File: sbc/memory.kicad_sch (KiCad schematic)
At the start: 6 parts, among them U10 AT27C256R, U11 IS61C5128AS-25QLI, U8 ATF22V10C, U9 ATF22V10C

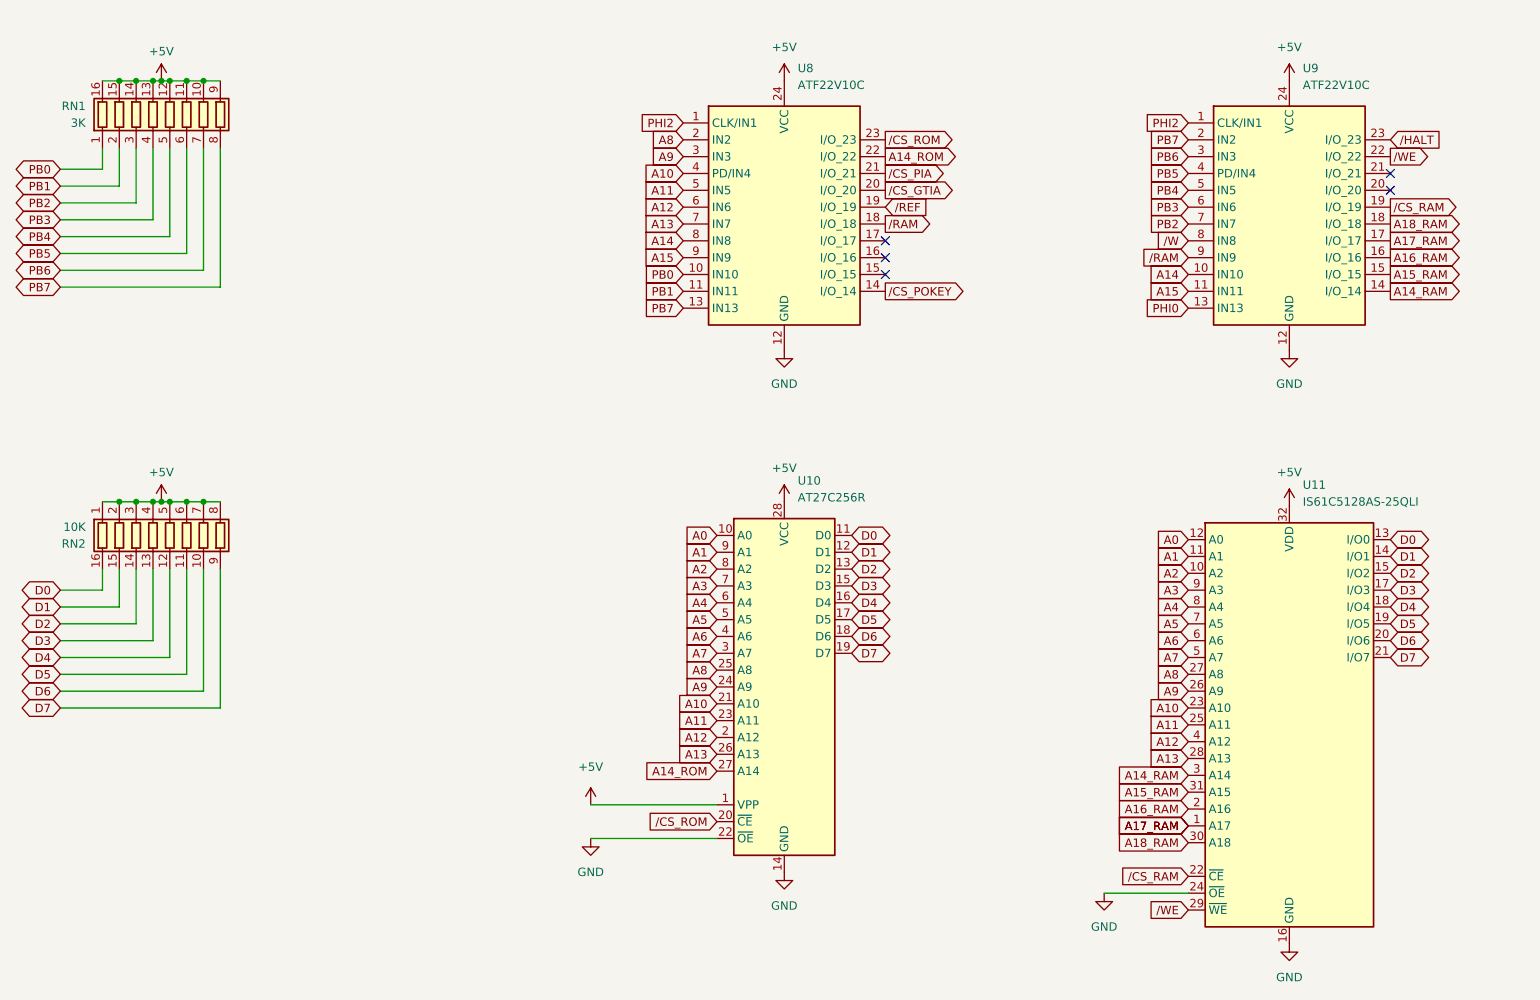
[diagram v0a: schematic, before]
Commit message: SBC v1.1
PCB fixes/changes:

  - Permanently power voltage translators
  - Conservatively specified a slower SRAM (the previous/faster SRAM does actually work fine)
  - RMU: Speculatively provided unbuffered PHI0 input and OE output (not actually needed)
  - Add pullups to open drain GTIA outputs
  - Plot selected values on silk screen
  - Accommodate KiCad 7 upgrade

- PLD changes:
  - Fix AMU logic
  - Fix RMU (unbuffered PHI0 and OE output not needed)

- QTPY firmware:
  - add soft power on/off support (Ctrl-F12)
  - reflects switched power and usb state in the neopixel
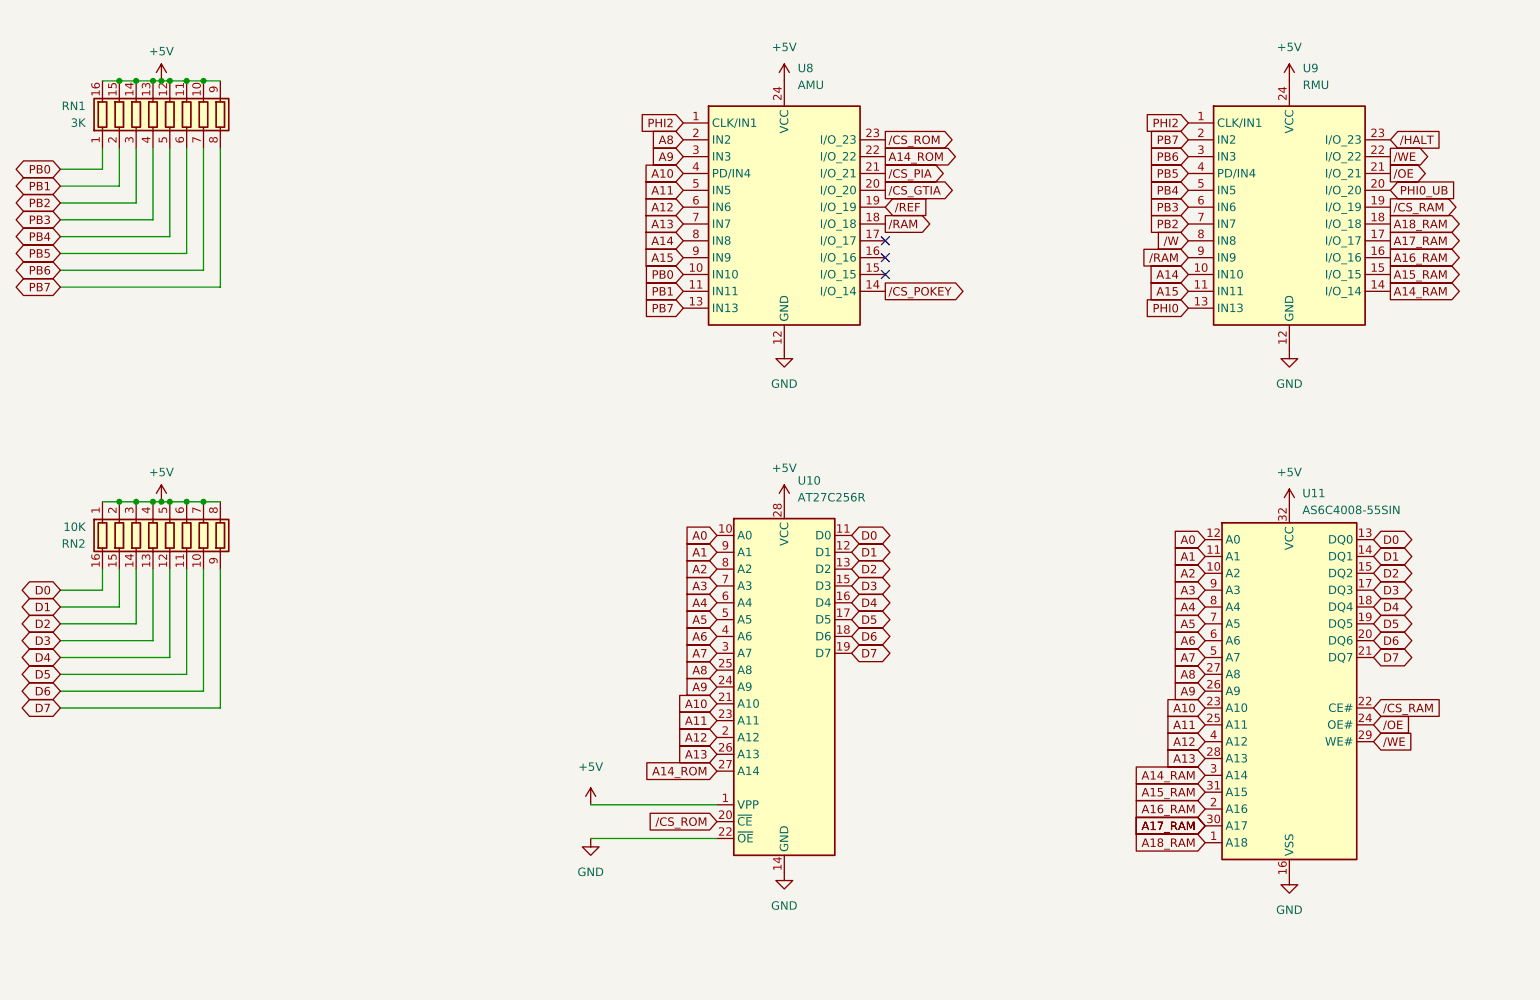
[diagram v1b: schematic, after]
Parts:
- removed U11: IS61C5128AS-25QLI, Package_SO:SSOP-32_11.305x20.495mm_P1.27mm, symbol Memory_RAM:IS61C5128AS-25QLI
- added U11: AS6C4008-55SIN, Package_SO:SSOP-32_11.305x20.495mm_P1.27mm, symbol Memory_RAM:AS6C4008-55PCN
- U8: value ATF22V10C -> AMU
- U9: value ATF22V10C -> RMU
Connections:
- net +5V: now also U11.32 (VCC)
- net A0: now also U11.12 (A0)
- net A1: now also U11.11 (A1)
- net A10: now also U11.23 (A10)
- net A11: now also U11.25 (A11)
- net A12: now also U11.4 (A12)
- net A13: now also U11.28 (A13)
- net A14_RAM: now also U11.3 (A14)
- net A15_RAM: now also U11.31 (A15)
- net A16_RAM: now also U11.2 (A16)
- net A17_RAM: now also U11.30 (A17)
- net A18_RAM: now also U11.1 (A18)
- net A2: now also U11.10 (A2)
- net A3: now also U11.9 (A3)
- net A4: now also U11.8 (A4)
- net A5: now also U11.7 (A5)
- net A6: now also U11.6 (A6)
- net A7: now also U11.5 (A7)
- net A8: now also U11.27 (A8)
- net A9: now also U11.26 (A9)
- net D0: now also U11.13 (DQ0)
- net D1: now also U11.14 (DQ1)
- net D2: now also U11.15 (DQ2)
- net D3: now also U11.17 (DQ3)
- net D4: now also U11.18 (DQ4)
- net D5: now also U11.19 (DQ5)
- net D6: now also U11.20 (DQ6)
- net D7: now also U11.21 (DQ7)
- net GND: now also U11.16 (VSS)
- net /CS_RAM: now also U11.22 (CE#)
- net /WE: now also U11.29 (WE#)
- net PHI0_UB: now reaches U9.20 (I/O_20)
- net /OE: now reaches U9.21 (I/O_21)
- net /OE: now also U11.24 (OE#)
- no-connect marks 5 -> 3

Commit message: SBC v1.2
SBC fixes/changes:

  - S-Video:
    - Fix S-Video footprint (Y and C swapped, and GNDs swapped) and adapt schematic to match
    - Wire S-Video grounds to AVA header instead of directly to (digital) GND
  - Audio:
    - Wire Audio-Out ground to AVA header
    - Drop SIO audio
    - Pullup open drain pokey audio
  - AMU/RMU:
    - Connect ROM and RAM OE to GND
    - Reserve AMU pin for "IO"
    - Reserve RMU pin for "antic" (registered halt)
    - Support for separate Antic banking (clock RMU with /phi2)
    - Supoprt 130XE and 320XE (compy)
  - Add the option for a resistor between OSC, PHI0 buffer and PHI2 buffer (to reduce over/under-shoot)
  - Invert CA2 (a PNP transistor on the Atari 800 XL inverts this signal)

Additions:

  - SBC Audio/Video board
  - SBC Case
  - SBC SD board

Stylize the complete system as "SFF 320XE".
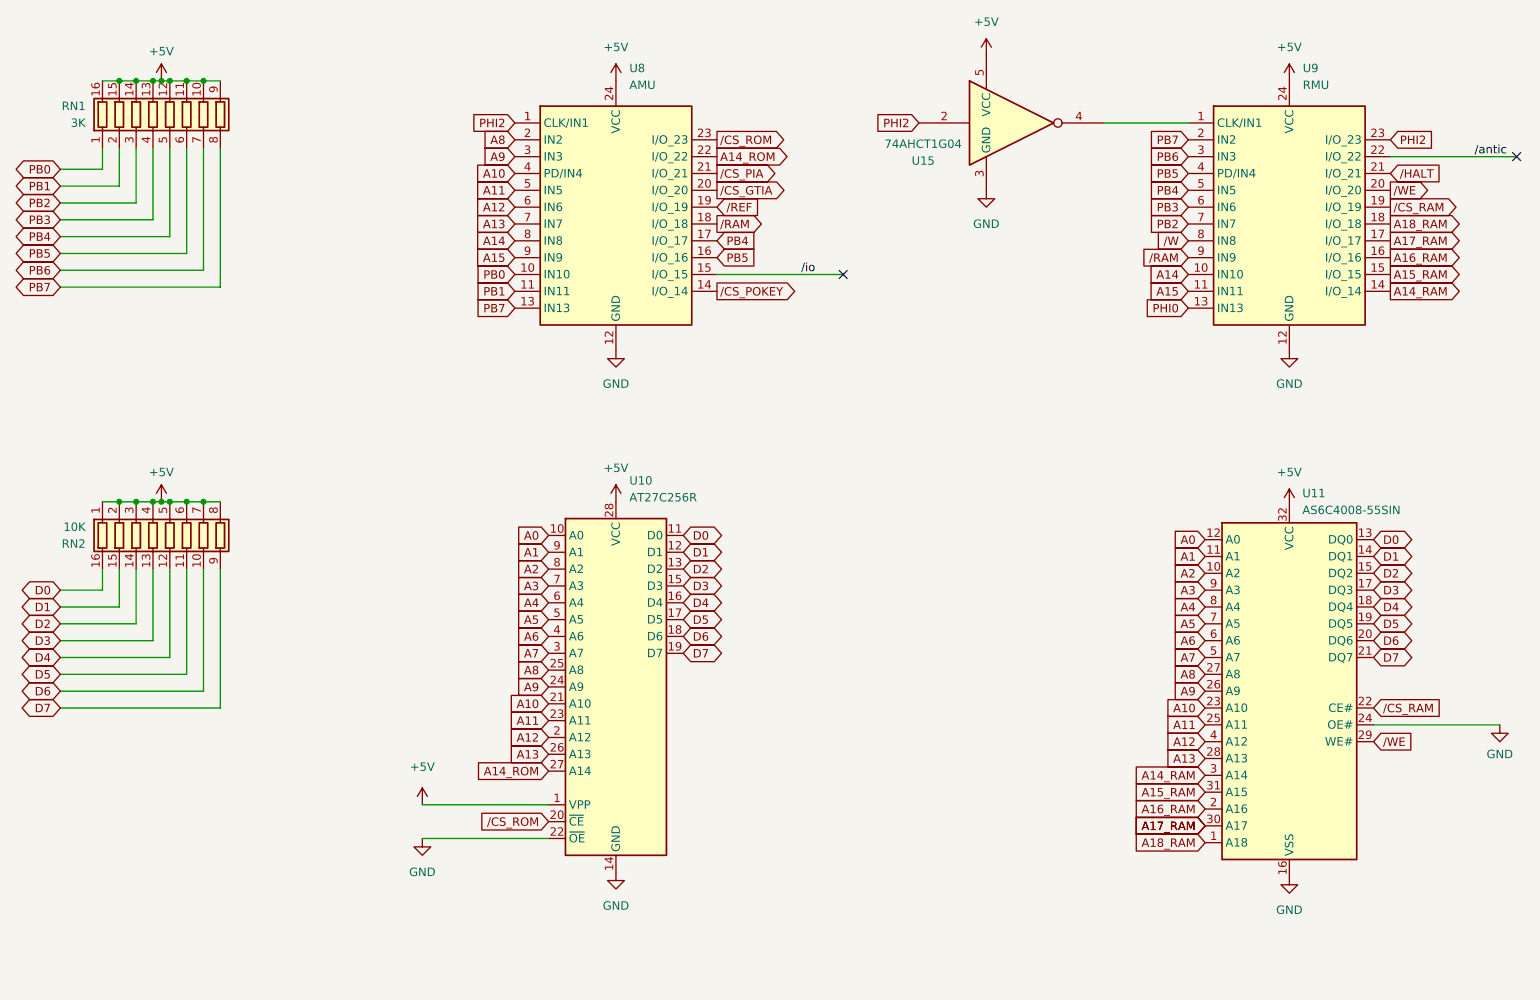
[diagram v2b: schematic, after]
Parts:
- added U15: 74AHCT1G04, Package_TO_SOT_SMD:SOT-23-5_HandSoldering, symbol 74xGxx:74AHCT1G04
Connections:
- net PHI0_UB is gone; now on net /WE: U9.20 (I/O_20)
- net +5V: now also U15.5 (VCC)
- net GND: now also U11.24 (OE#), U15.3 (GND)
- net PB4: now also U8.17 (I/O_17)
- net PB5: now also U8.16 (I/O_16)
- net PHI2: now also U9.23 (I/O_23), U15.2; no longer U9.1 (CLK/IN1)
- net /HALT: now also U9.21 (I/O_21); no longer U9.23 (I/O_23)
- net /WE: no longer U9.22 (I/O_22)
- net /io: now reaches U8.15 (I/O_15)
- removed net /OE: U11.24 (OE#), U9.21 (I/O_21)
- new net: U15.4, U9.1 (CLK/IN1)
- new net /antic: U9.22 (I/O_22)
- no-connect marks 3 -> 2
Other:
- moved on the sheet: U10, U8

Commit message: SBC v1.3
Motherboard updates:

  - KiCad 9 upgrade
  - USB-C power connector
  - Replace EOL resistor packs with discrete SMD resistors
  - Power/enable voltage translators from switched 5V
  - Fix motor signal pullup
  - Eliminate loop in phi2 traces
  - Thicker clock signal traces

SD card adapter updates:

  - KiCad 9 upgrade
  - Power/enable voltage translator from switched 5V and the eliminate unnecessary SIO pullups

Audio/Video adapter updates:

  - KiCad 9 upgrade
  - No functional changes, gerbers not regenerated, cleaned up bom
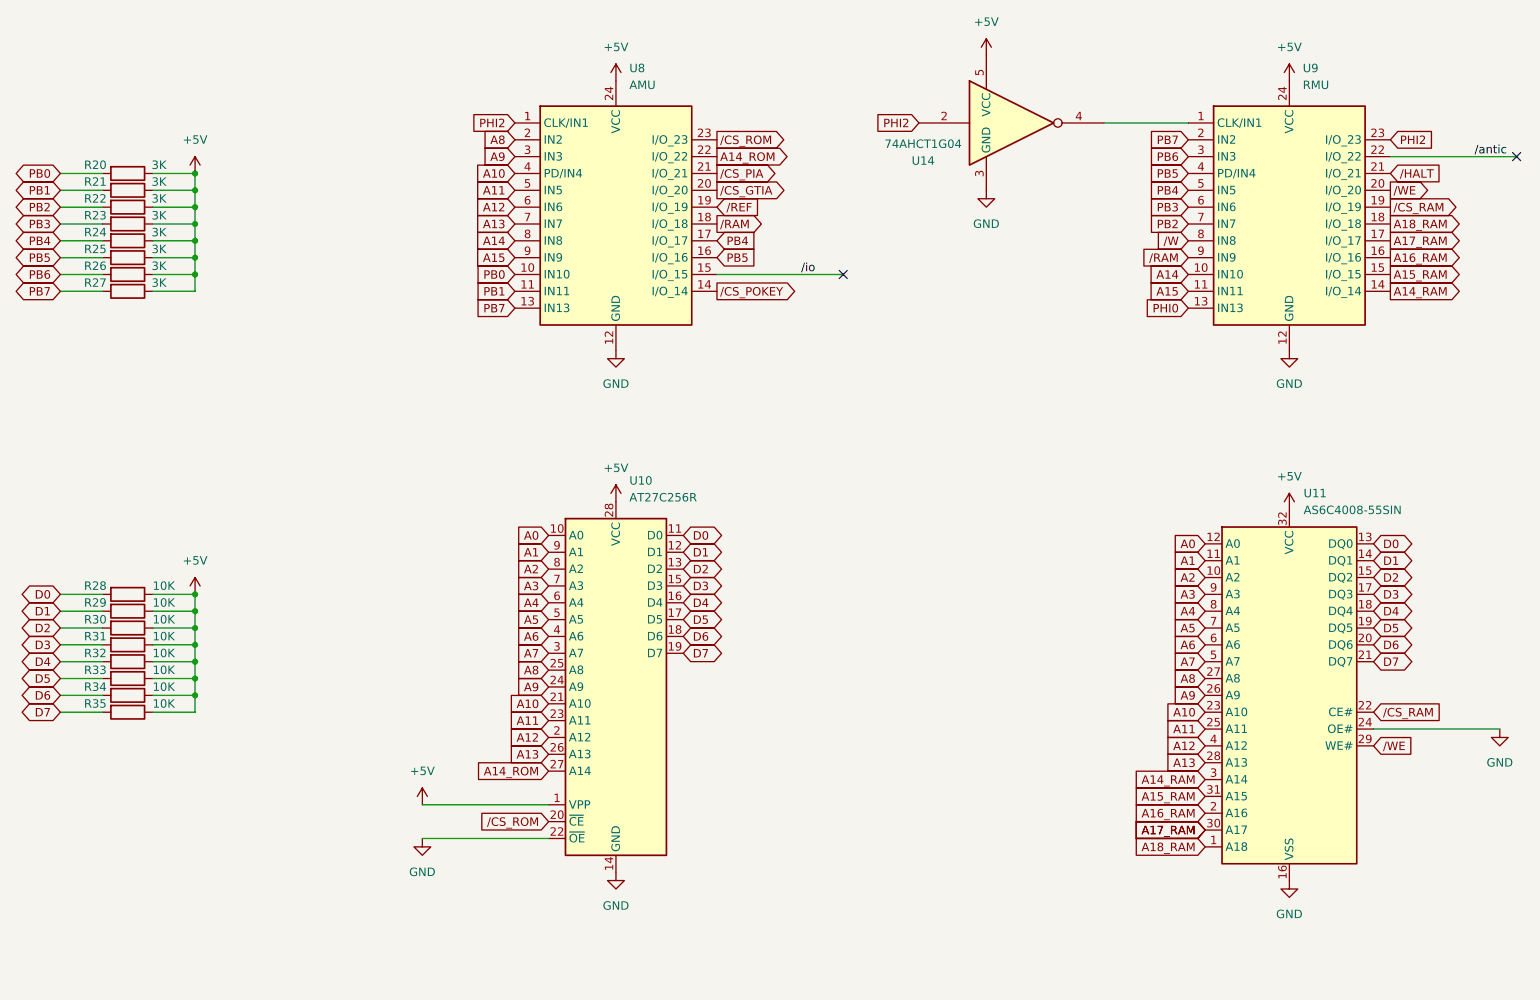
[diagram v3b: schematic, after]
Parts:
- removed RN1: 3K, Package_SO:SOIC-16W_5.3x10.2mm_P1.27mm, symbol Device:R_Pack08
- removed RN2: 10K, Package_SO:SOIC-16_3.9x9.9mm_P1.27mm, symbol Device:R_Pack08
- added R20, R21, R22, R23, R24, R25, R26, R27: 3K, Resistor_SMD:R_0805_2012Metric_Pad1.20x1.40mm_HandSolder, symbol Device:R
- added R28, R29, R30, R31, R32, R33, R34, R35: 10K, Resistor_SMD:R_0805_2012Metric_Pad1.20x1.40mm_HandSolder, symbol Device:R
- U11: footprint Package_SO:SSOP-32_11.305x20.495mm_P1.27mm -> Package_SO:SOP-32_11.305x20.495mm_P1.27mm
- renumbered U15 to U14
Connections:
- net +5V: now also R20.1, R21.1, R22.1, R23.1, R24.1, R25.1, R26.1, R27.1, R28.1, R29.1, R30.1, R31.1, R32.1, R33.1, R34.1, R35.1
- net D0: now also R28.2
- net D1: now also R29.2
- net D2: now also R30.2
- net D3: now also R31.2
- net D4: now also R32.2
- net D5: now also R33.2
- net D6: now also R34.2
- net D7: now also R35.2
- net PB0: now also R20.2
- net PB1: now also R21.2
- net PB2: now also R22.2
- net PB3: now also R23.2
- net PB4: now also R24.2
- net PB5: now also R25.2
- net PB6: now also R26.2
- net PB7: now also R27.2
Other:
- moved on the sheet: U11
